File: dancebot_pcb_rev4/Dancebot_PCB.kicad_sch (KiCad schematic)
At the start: 4 parts

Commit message: schematic ready for review!
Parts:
- H1, H2, H3, H5: footprint (none) -> MountingHole:MountingHole_3.2mm_M3; symbol Mechanical:MountingHole_Pad -> Mechanical:MountingHole
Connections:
- removed net GND: H1.1, H2.1, H3.1, H5.1

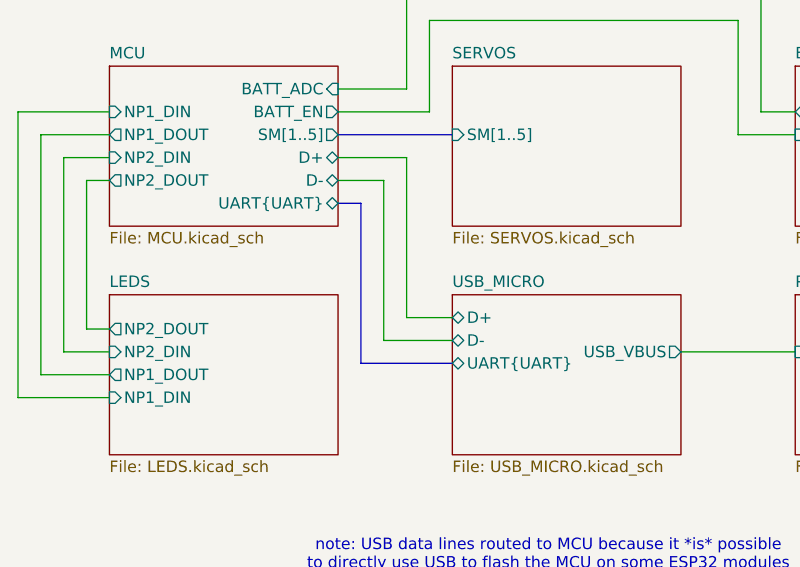
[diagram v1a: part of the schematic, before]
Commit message: now using ESP32-S3-WROOM-1, changed power delivery system
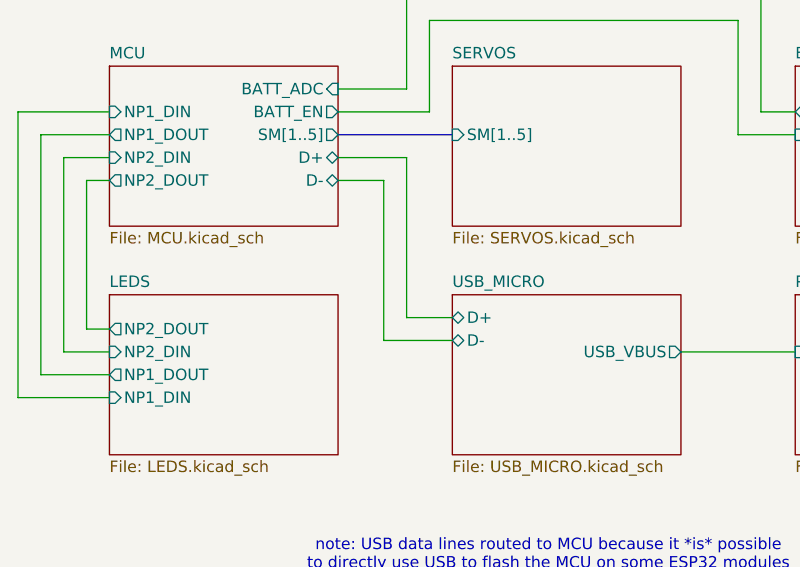
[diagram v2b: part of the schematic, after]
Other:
- sheet MCU ports: added none; removed UART{UART}
- sheet USB_MICRO ports: added none; removed UART{UART}
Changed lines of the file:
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@@
+		)
+	)
+	(wire
+		(pts
+			(xy 77.47 105.41) (xy 67.31 105.41)
+		)
+		(stroke
+			(width 0)
+			(type default)
 		)
 	)
 	(bus
 		(pts
-			(xy 105.41 101.6) (xy 105.41 83.82)
-		)
-		(stroke
-			(width 0)
-			(type default)
-		)
-	)
-	(wire
-		(pts
-			(xy 77.47 105.41) (xy 67.31 105.41)
-		)
-		(stroke
-			(width 0)
-			(type default)
-		)
-	)
-	(bus
-		(pts
 			(xy 102.87 76.2) (xy 115.57 76.2)
 		)
@@
 		(pts
 			(xy 147.32 76.2) (xy 153.67 76.2)
-		)
-		(stroke
-			(width 0)
-			(type default)
-		)
-	)
-	(bus
-		(pts
-			(xy 115.57 101.6) (xy 105.41 101.6)
-		)
-		(stroke
-			(width 0)
-			(type default)
-		)
-	)
-	(bus
-		(pts
-			(xy 105.41 83.82) (xy 102.87 83.82)
 		)
 		(stroke
@@
 			)
 		)
-		(pin "UART{UART}" bidirectional
-			(at 102.87 83.82 0)
-			(effects
-				(font
-					(size 1.27 1.27)
-				)
-				(justify right)
-			)
-		)
 		(pin "NP1_DIN" input
 			(at 77.47 73.66 180)
@@
 			(effects
 				(font
-					(size 1.27 1.27)
-				)
-				(justify left)
-			)
-		)
-		(pin "UART{UART}" bidirectional
-			(at 115.57 101.6 180)
-			(effects
-				(font

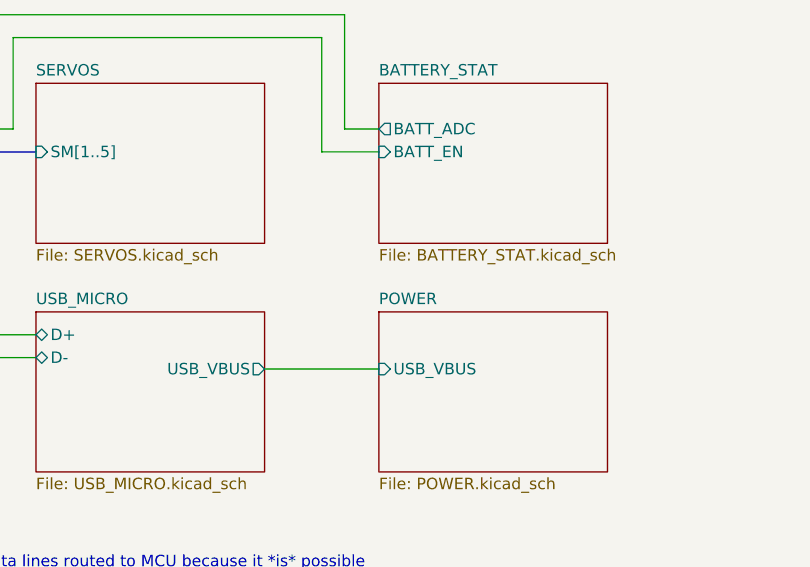
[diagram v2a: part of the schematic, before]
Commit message: fixed some issues with labels
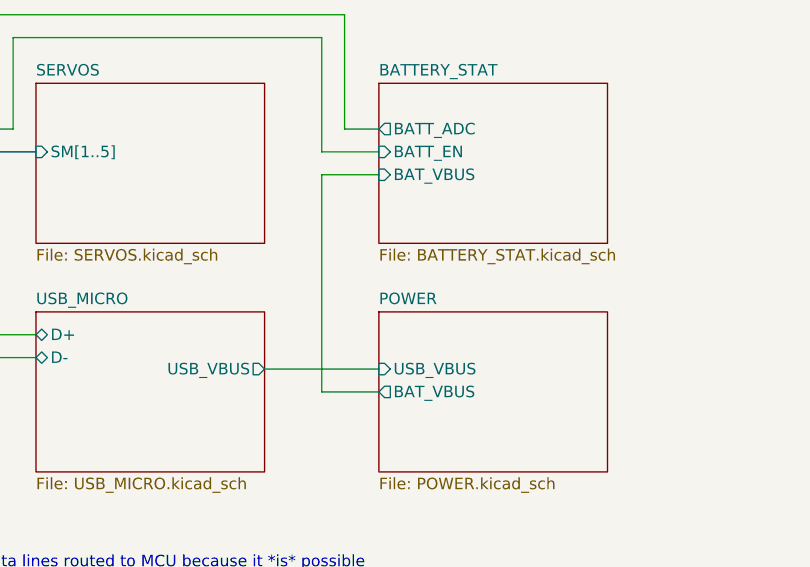
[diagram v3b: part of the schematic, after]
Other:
- sheet BATTERY_STAT ports: added BAT_VBUS; removed none
- sheet POWER ports: added BAT_VBUS; removed none
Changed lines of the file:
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@@
+	(wire
+		(pts
+			(xy 147.32 102.87) (xy 153.67 102.87)
+		)
+		(stroke
+			(width 0)
+			(type default)
+		)
+	)
 	(wire
 		(pts
@@
 		(pts
 			(xy 147.32 76.2) (xy 153.67 76.2)
+		)
+		(stroke
+			(width 0)
+			(type default)
+		)
+	)
+	(wire
+		(pts
+			(xy 153.67 78.74) (xy 147.32 78.74)
+		)
+		(stroke
+			(width 0)
+			(type default)
+		)
+	)
+	(wire
+		(pts
+			(xy 147.32 78.74) (xy 147.32 102.87)
 		)
 		(stroke
@@
 			)
 		)
+		(pin "BAT_VBUS" output
+			(at 153.67 102.87 180)
+			(effects
+				(font
+					(size 1.27 1.27)
+				)
+				(justify left)
+			)
+		)
 		(instances
 			(project "Dancebot_PCB"
@@
 			(effects
 				(font
+					(size 1.27 1.27)
+				)
+				(justify left)
+			)
+		)
+		(pin "BAT_VBUS" input
+			(at 153.67 78.74 180)
+			(effects
+				(font

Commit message: implemented some changes
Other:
- sheet LEDS ports: added IO45; removed none
- sheet MCU ports: added IO45; removed none
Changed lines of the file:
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@@
+	(wire
+		(pts
+			(xy 64.77 107.95) (xy 77.47 107.95)
+		)
+		(stroke
+			(width 0)
+			(type default)
+		)
+	)
 	(wire
 		(pts
@@
 	(wire
 		(pts
+			(xy 64.77 71.12) (xy 64.77 107.95)
+		)
+		(stroke
+			(width 0)
+			(type default)
+		)
+	)
+	(wire
+		(pts
 			(xy 153.67 73.66) (xy 149.86 73.66)
 		)
@@
 		(pts
 			(xy 74.93 81.28) (xy 74.93 97.79)
+		)
+		(stroke
+			(width 0)
+			(type default)
+		)
+	)
+	(wire
+		(pts
+			(xy 77.47 71.12) (xy 64.77 71.12)
 		)
 		(stroke
@@
 			)
 		)
+		(pin "IO45" output
+			(at 77.47 71.12 180)
+			(effects
+				(font
+					(size 1.27 1.27)
+				)
+				(justify left)
+			)
+		)
 		(instances
 			(project "Dancebot_PCB"
@@
 			(effects
 				(font
+					(size 1.27 1.27)
+				)
+				(justify left)
+			)
+		)
+		(pin "IO45" input
+			(at 77.47 107.95 180)
+			(effects
+				(font

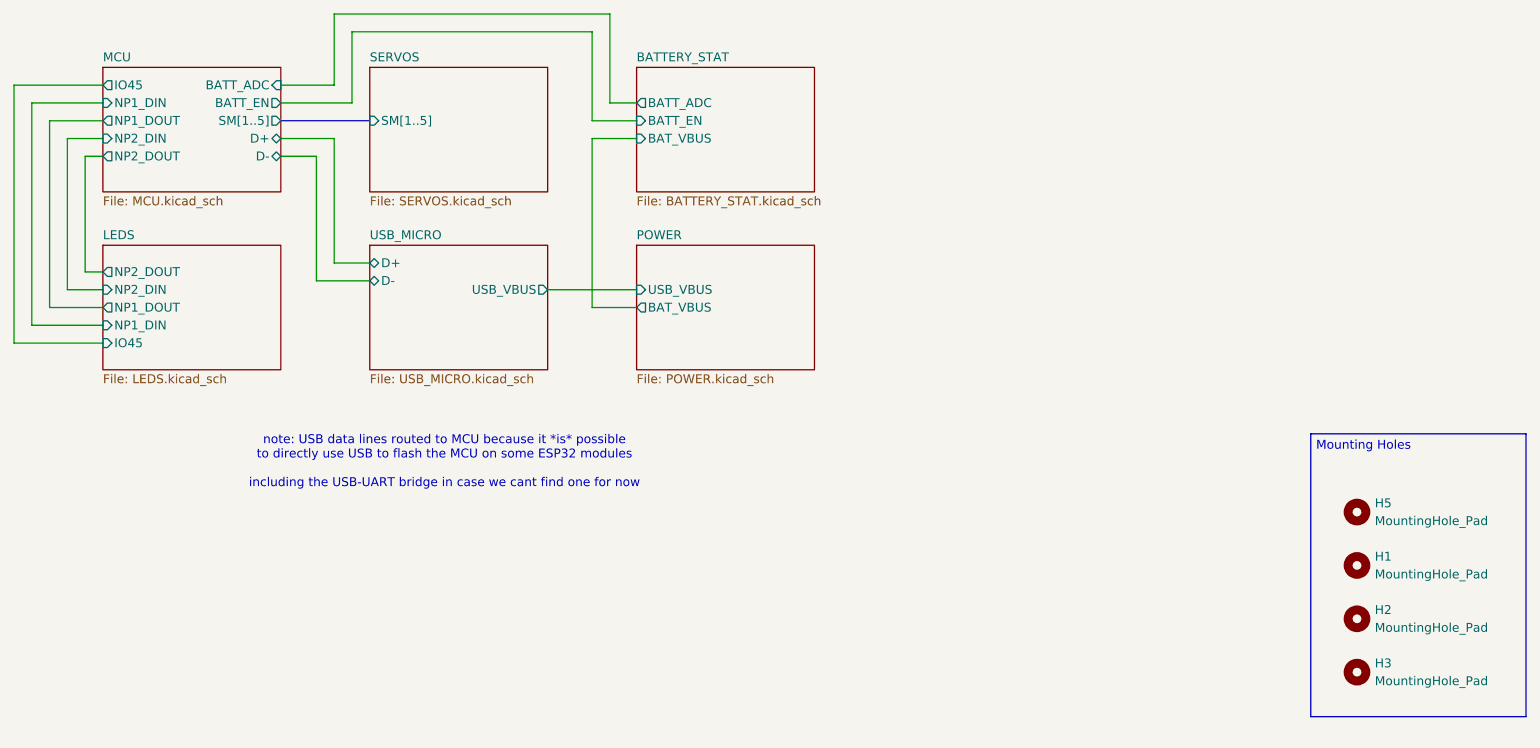
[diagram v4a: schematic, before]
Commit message: added more power leds. need to finish routing. fixed 3d models
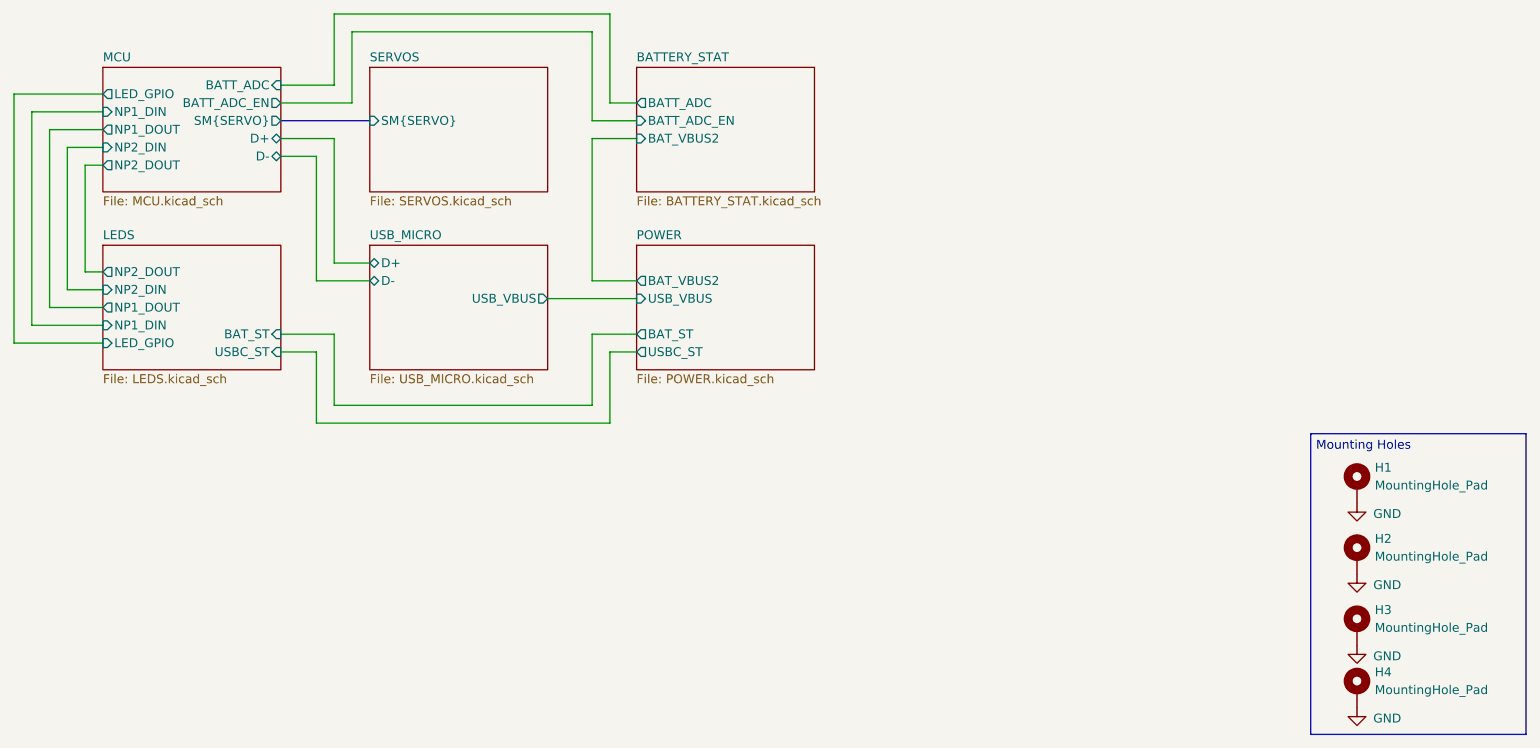
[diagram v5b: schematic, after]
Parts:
- H1: renamed from H5; footprint MountingHole:MountingHole_3.2mm_M3 -> MountingHole:MountingHole_3.2mm_M3_ISO7380_Pad; symbol Mechanical:MountingHole -> SamacSys_Parts:MountingHole_Pad_MP
- H2: renamed from H1; footprint MountingHole:MountingHole_3.2mm_M3 -> MountingHole:MountingHole_3.2mm_M3_ISO7380_Pad; symbol Mechanical:MountingHole -> SamacSys_Parts:MountingHole_Pad_MP
- H3: renamed from H2; footprint MountingHole:MountingHole_3.2mm_M3 -> MountingHole:MountingHole_3.2mm_M3_ISO7380_Pad; symbol Mechanical:MountingHole -> SamacSys_Parts:MountingHole_Pad_MP
- H4: renamed from H3; footprint MountingHole:MountingHole_3.2mm_M3 -> MountingHole:MountingHole_3.2mm_M3_ISO7380_Pad; symbol Mechanical:MountingHole -> SamacSys_Parts:MountingHole_Pad_MP
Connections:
- new net GND: H1.1, H2.1, H3.1, H4.1
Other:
- sheet BATTERY_STAT ports: added BATT_ADC_EN, BAT_VBUS2; removed BATT_EN, BAT_VBUS
- sheet LEDS ports: added BAT_ST, LED_GPIO, USBC_ST; removed IO45
- sheet MCU ports: added BATT_ADC_EN, LED_GPIO, SM{SERVO}; removed BATT_EN, IO45, SM[1..5]
- sheet POWER ports: added BAT_ST, BAT_VBUS2, USBC_ST; removed BAT_VBUS
- sheet SERVOS ports: added SM{SERVO}; removed SM[1..5]
- note removed: "note: USB data lines routed to MCU because it *is* possible to directly use USB to flash the MCU on some ESP32 modules including the USB-UART bridge in case we cant find one for now"
